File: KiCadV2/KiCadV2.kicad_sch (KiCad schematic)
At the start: 52 parts, among them J1 USB_C_Receptacle_PowerOnly_6P, J3 Screw_Terminal_01x02, J4 Screw_Terminal_01x02, U1 MT3608, U14 74LV08AT14-13, U16 NC7SZ157P6X, U17 MX3502S, U18 MX3502S, U2 74HC595, U26 MX3502S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

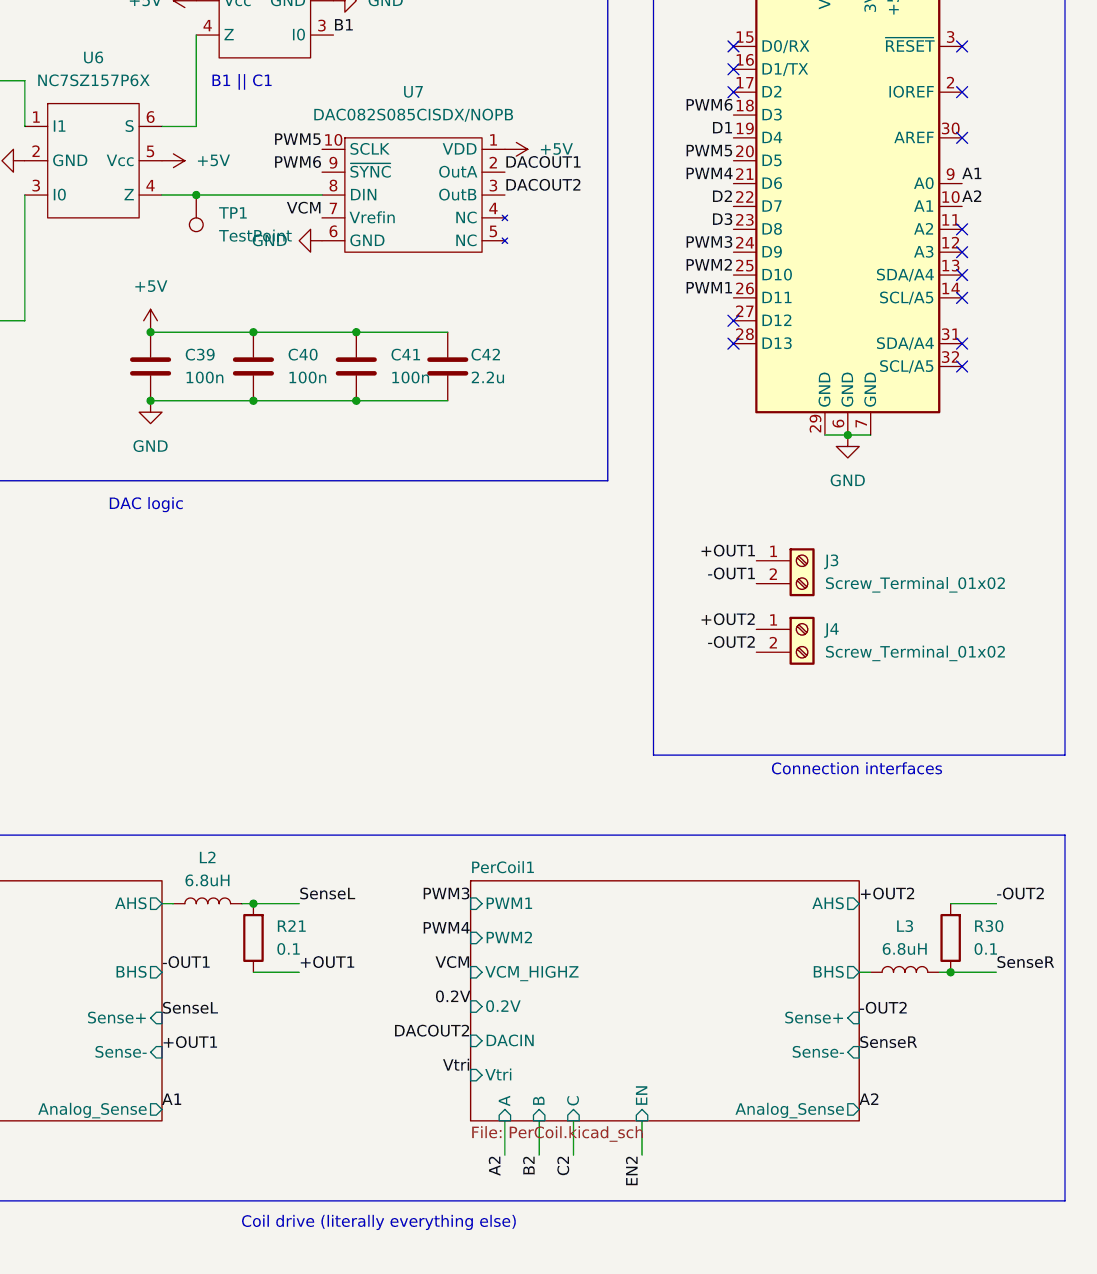
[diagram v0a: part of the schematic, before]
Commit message: minor bug
whoops! Mixed up my Analog pins A1 & A2 with my state pins A1 & A2. That would've been bad 😅
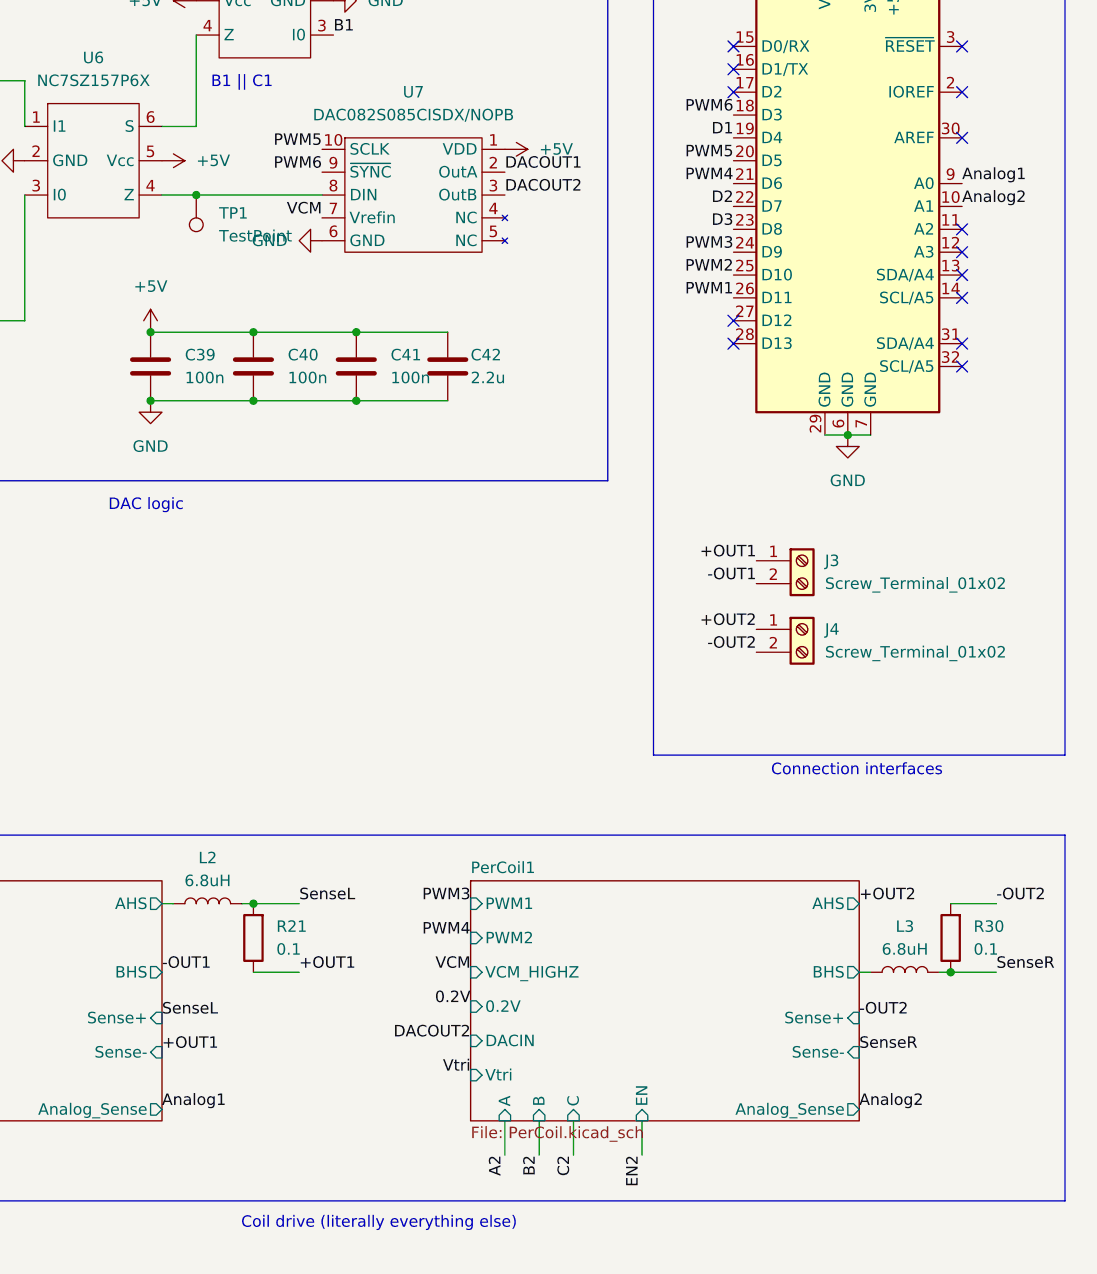
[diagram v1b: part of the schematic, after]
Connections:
- net A1: no longer A1.9 (A0)
- net A2: no longer A1.10 (A1)
- new net Analog1: A1.9 (A0)
- new net Analog2: A1.10 (A1)
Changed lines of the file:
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@@
 		)
 	)
-	(label "A1"
+	(label "Analog1"
 		(at 184.15 148.59 0)
 		(effects
@@
 		)
 	)
+	(label "Analog2"
+		(at 273.05 48.26 0)
+		(effects
+			(font
+				(size 1.27 1.27)
+			)
+			(justify left bottom)
+		)
+	)
 	(label "-OUT1"
 		(at 250.19 90.17 180)
@@
 		)
 	)
-	(label "A2"
-		(at 273.05 48.26 0)
-		(effects
-			(font
-				(size 1.27 1.27)
-			)
-			(justify left bottom)
-		)
-	)
 	(label "VCM"
 		(at 218.44 133.35 180)
@@
 	(label "C2"
 		(at 113.03 46.99 0)
-		(effects
-			(font
-				(size 1.27 1.27)
-			)
-			(justify left bottom)
-		)
-	)
-	(label "A1"
-		(at 273.05 45.72 0)
 		(effects
 			(font
@@
 	)
 	(label "SenseR"
+		(at 276.86 133.35 0)
+		(effects
+			(font
+				(size 1.27 1.27)
+			)
+			(justify left bottom)
+		)
+	)
+	(label "SenseR"
 		(at 261.62 142.24 0)
-		(effects
-			(font
-				(size 1.27 1.27)
-			)
-			(justify left bottom)
-		)
-	)
-	(label "SenseR"
-		(at 276.86 133.35 0)
 		(effects
 			(font
@@
 		)
 	)
+	(label "Analog1"
+		(at 273.05 45.72 0)
+		(effects
+			(font
+				(size 1.27 1.27)
+			)
+			(justify left bottom)
+		)
+	)
 	(label "-OUT2"
 		(at 261.62 138.43 0)
@@
 		)
 	)
-	(label "A2"
+	(label "Analog2"
 		(at 261.62 148.59 0)
 		(effects

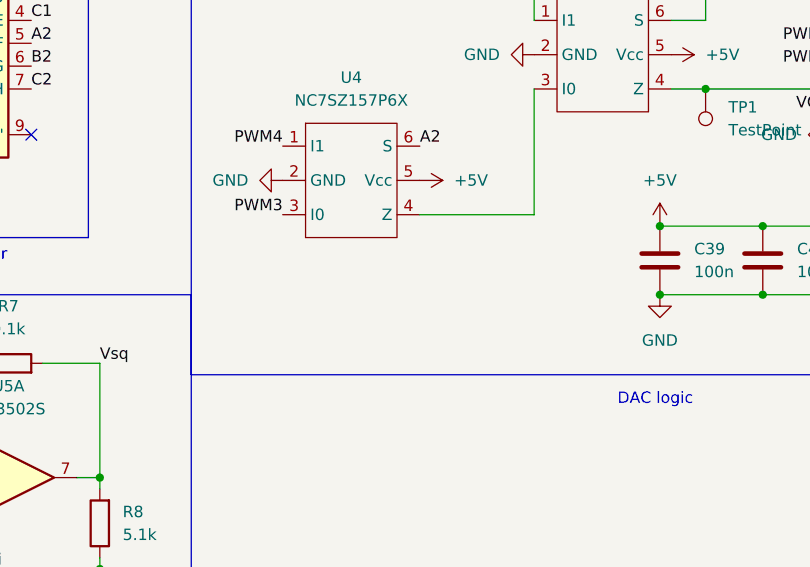
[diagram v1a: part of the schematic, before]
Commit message: DAC logic
- Internal connections done
- Spacing, shorts, nets, etc verified
- Grouped
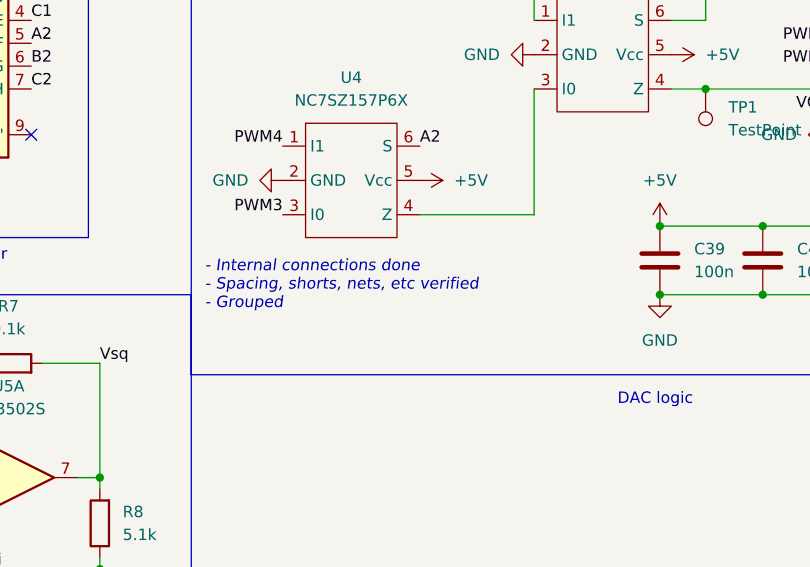
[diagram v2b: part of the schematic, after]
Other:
- note added: "- Internal connections done - Spacing, shorts, nets, etc verified - Grouped"
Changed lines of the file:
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@@
+		)
+	)
+	(text "- Internal connections done\n- Spacing, shorts, nets, etc verified\n- Grouped"
+		(exclude_from_sim no)
+		(at 132.334 68.834 0)
+		(effects
+			(font
+				(size 1.27 1.27)
+				(italic yes)
+				(color 0 194 0 1)
+			)
+			(justify left)
 		)
 	)

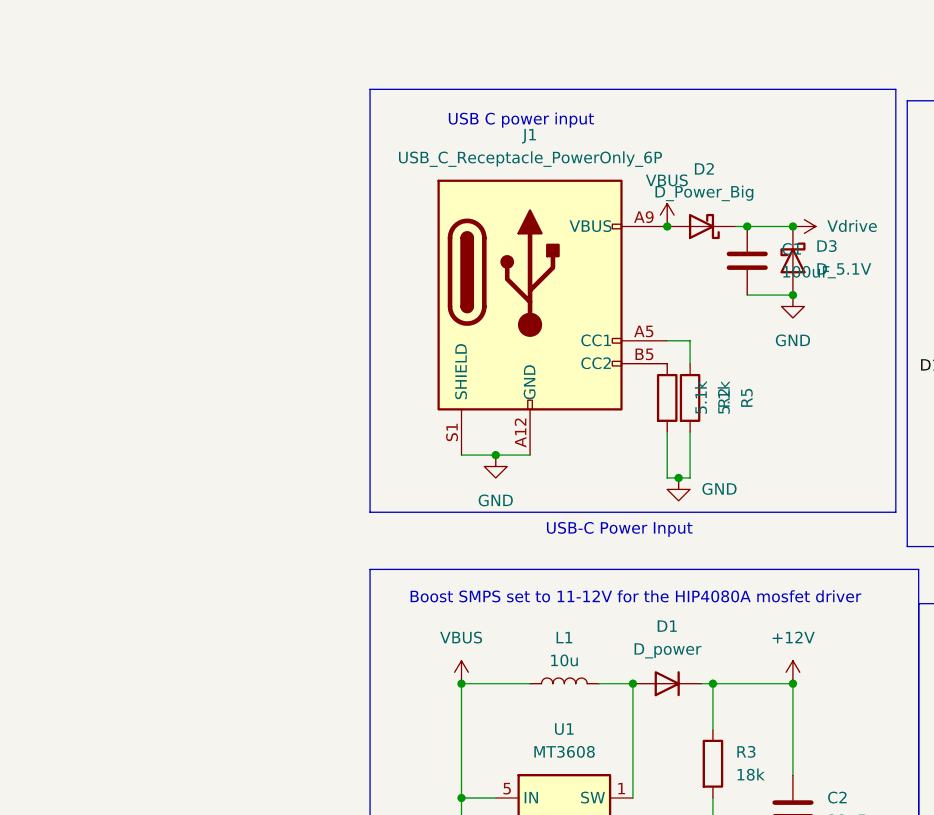
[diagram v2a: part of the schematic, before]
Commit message: USBC power & Boost SMPS done
- Internal connections done
- Spacing, shorts, nets, etc verified
- Grouped
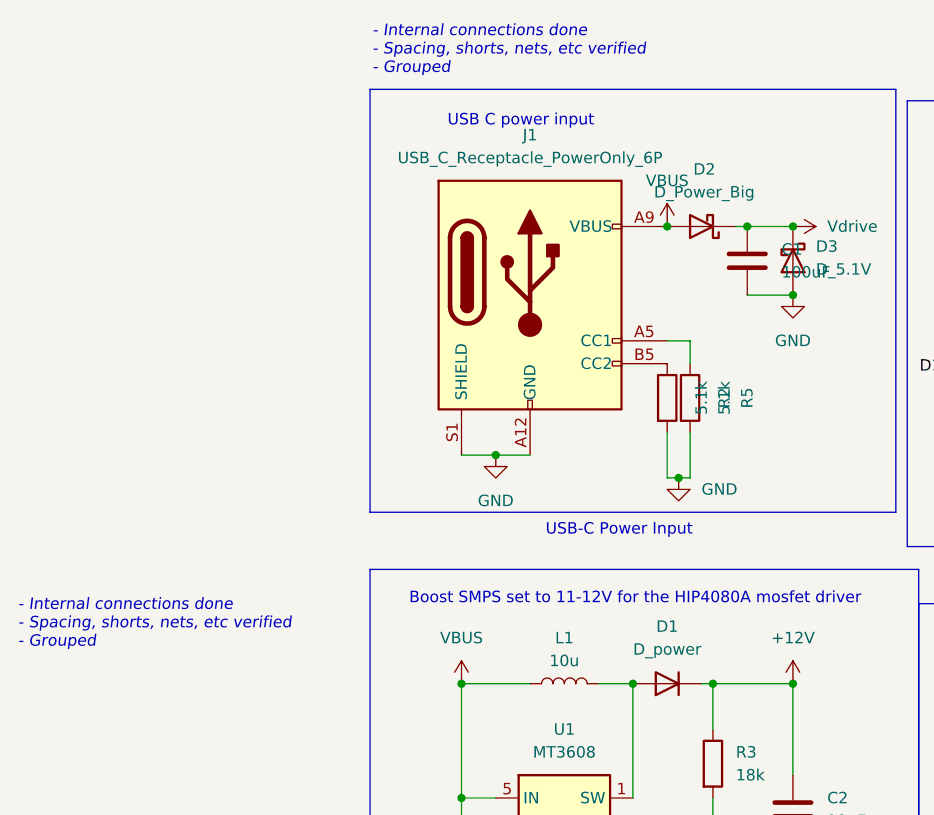
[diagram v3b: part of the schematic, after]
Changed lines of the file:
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@@
+		)
+	)
+	(text "- Internal connections done\n- Spacing, shorts, nets, etc verified\n- Grouped"
+		(exclude_from_sim no)
+		(at -26.416 72.136 0)
+		(effects
+			(font
+				(size 1.27 1.27)
+				(italic yes)
+				(color 0 194 0 1)
+			)
+			(justify left)
 		)
 	)
@@
 		)
 	)
+	(text "- Internal connections done\n- Spacing, shorts, nets, etc verified\n- Grouped"
+		(exclude_from_sim no)
+		(at 12.954 8.382 0)
+		(effects
+			(font
+				(size 1.27 1.27)
+				(italic yes)
+				(color 0 194 0 1)
+			)
+			(justify left)
+		)
+	)

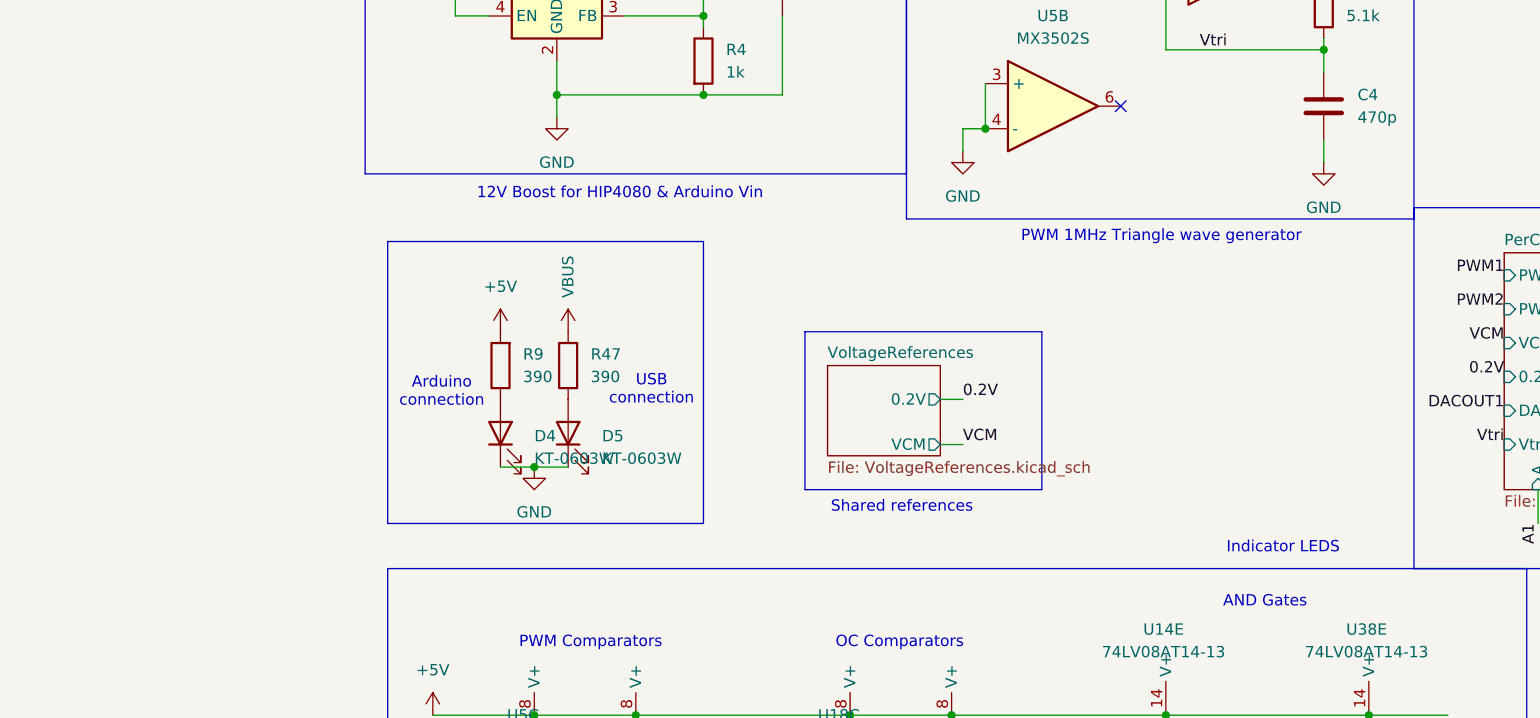
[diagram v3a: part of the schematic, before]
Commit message: Triangle wave done
- Internal connections done
- Spacing, shorts, nets, etc verified
- Grouped
*Doesn't fit now...
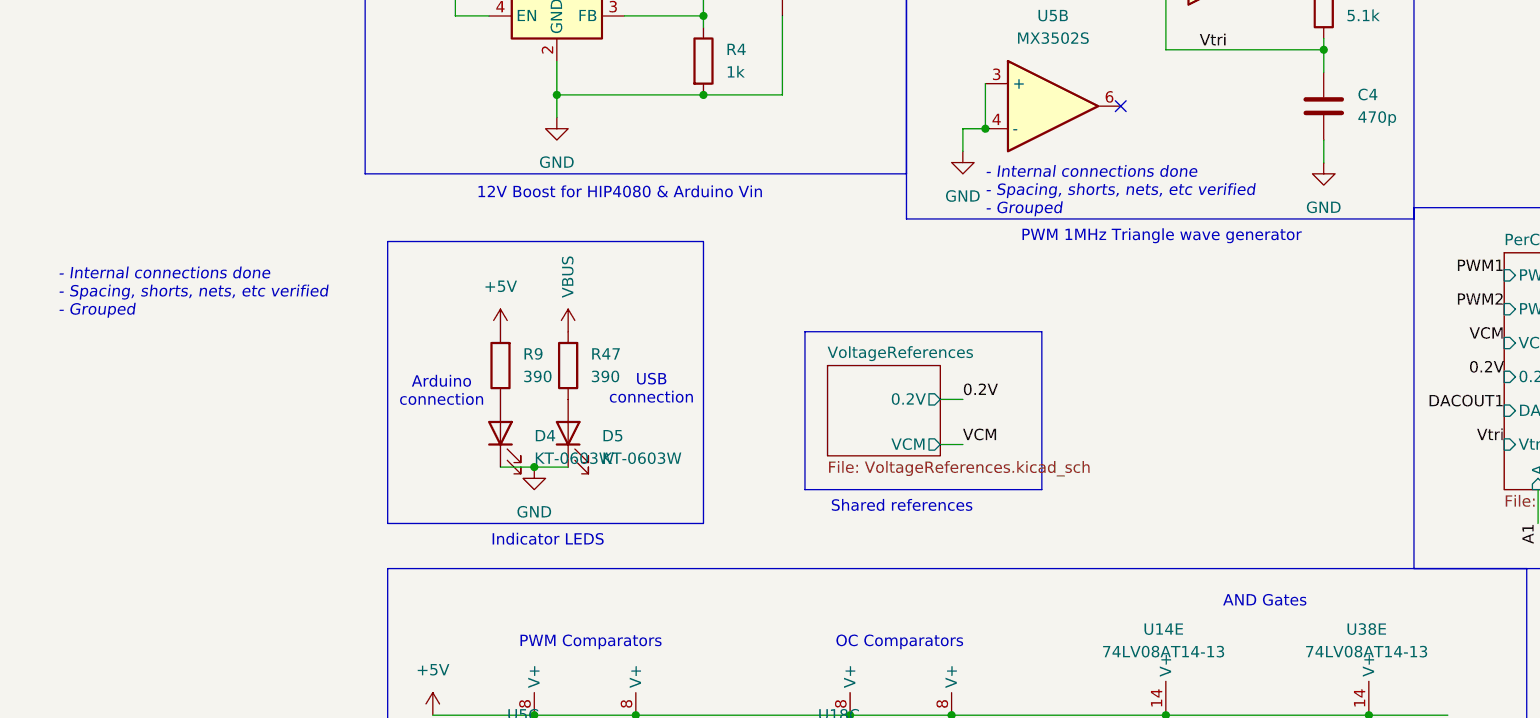
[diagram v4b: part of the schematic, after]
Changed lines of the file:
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@@
+		)
+	)
+	(text "- Internal connections done\n- Spacing, shorts, nets, etc verified\n- Grouped"
+		(exclude_from_sim no)
+		(at 82.55 116.332 0)
+		(effects
+			(font
+				(size 1.27 1.27)
+				(italic yes)
+				(color 0 194 0 1)
+			)
+			(justify left)
 		)
 	)
@@
 	(text "Indicator LEDS"
 		(exclude_from_sim no)
-		(at 116.078 156.464 0)
+		(at 33.274 155.702 0)
 		(effects
 			(font
@@
 		)
 	)
+	(text "- Internal connections done\n- Spacing, shorts, nets, etc verified\n- Grouped"
+		(exclude_from_sim no)
+		(at -21.844 127.762 0)
+		(effects
+			(font
+				(size 1.27 1.27)
+				(italic yes)
+				(color 0 194 0 1)
+			)
+			(justify left)
+		)
+	)

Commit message: Bunchhh of shit
PCB looking gooood
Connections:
- net PWM1: now also A1.20 (D5); no longer A1.26 (D11)
- net PWM2: now also A1.18 (D3); no longer A1.25 (D10)
- net PWM5: now also A1.26 (D11); no longer A1.20 (D5)
- net PWM6: now also A1.25 (D10); no longer A1.18 (D3)
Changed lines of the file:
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@@
 		)
 	)
-	(label "PWM6"
+	(label "PWM2"
 		(at 247.65 38.1 180)
 		(effects
@@
 		)
 	)
-	(label "PWM5"
+	(label "PWM1"
 		(at 247.65 43.18 180)
 		(effects
@@
 		)
 	)
-	(label "PWM1"
+	(label "PWM5"
 		(at 247.65 58.42 180)
 		(effects
@@
 		)
 	)
-	(label "PWM2"
+	(label "PWM6"
 		(at 247.65 55.88 180)
 		(effects

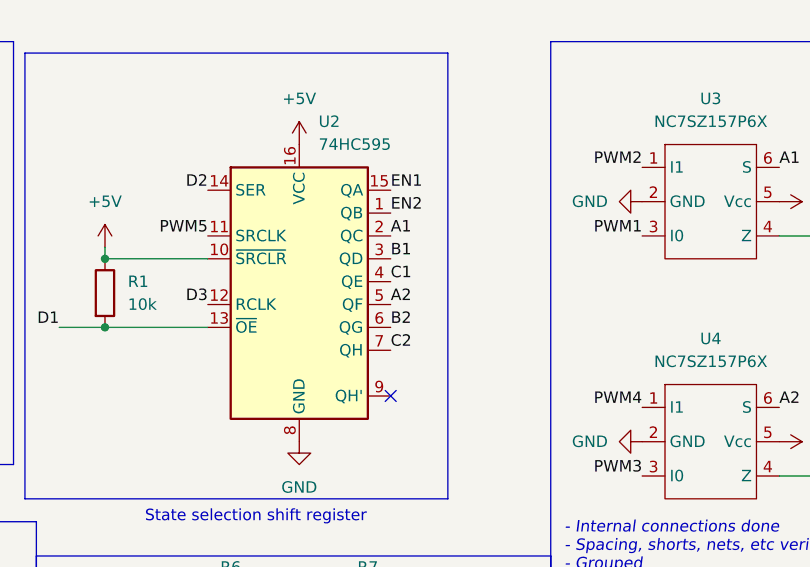
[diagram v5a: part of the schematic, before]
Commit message: Only GND via stitching left!!!
OMG OMG OMG PLEASE NO HUGE ERRORS
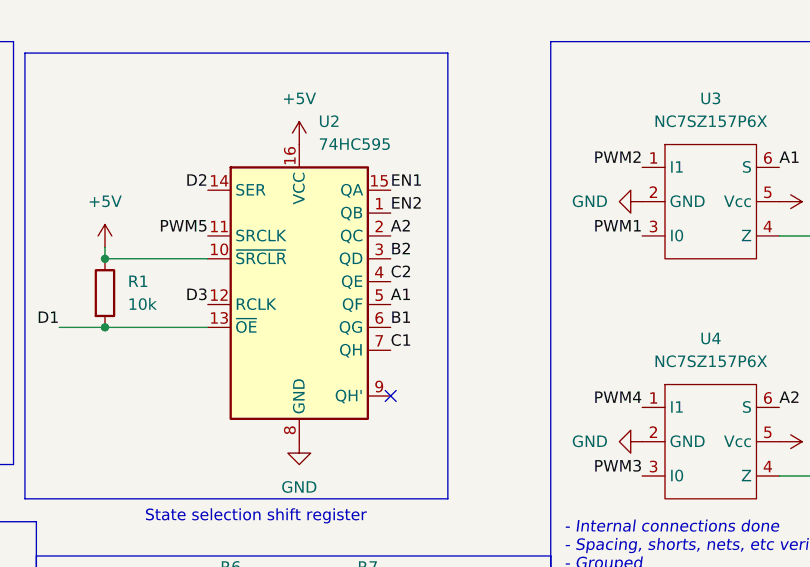
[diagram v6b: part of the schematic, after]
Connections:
- net A1: now also U2.5 (QF); no longer U2.2 (QC)
- net A2: now also U2.2 (QC); no longer U2.5 (QF)
- net B1: now also U2.6 (QG); no longer U2.3 (QD)
- net B2: now also U2.3 (QD); no longer U2.6 (QG)
- net C1: now also U2.7 (QH); no longer U2.4 (QE)
- net C2: now also U2.4 (QE); no longer U2.7 (QH)
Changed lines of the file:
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@@
 	)
 	(label "A1"
+		(at 113.03 41.91 0)
+		(effects
+			(font
+				(size 1.27 1.27)
+			)
+			(justify left bottom)
+		)
+	)
+	(label "B1"
+		(at 113.03 44.45 0)
+		(effects
+			(font
+				(size 1.27 1.27)
+			)
+			(justify left bottom)
+		)
+	)
+	(label "C1"
+		(at 113.03 46.99 0)
+		(effects
+			(font
+				(size 1.27 1.27)
+			)
+			(justify left bottom)
+		)
+	)
+	(label "A2"
 		(at 113.03 34.29 0)
 		(effects
@@
 		)
 	)
-	(label "B1"
+	(label "B2"
 		(at 113.03 36.83 0)
-		(effects
-			(font
-				(size 1.27 1.27)
-			)
-			(justify left bottom)
-		)
-	)
-	(label "C1"
-		(at 113.03 39.37 0)
-		(effects
-			(font
-				(size 1.27 1.27)
-			)
-			(justify left bottom)
-		)
-	)
-	(label "A2"
-		(at 113.03 41.91 0)
-		(effects
-			(font
-				(size 1.27 1.27)
-			)
-			(justify left bottom)
-		)
-	)
-	(label "B2"
-		(at 113.03 44.45 0)
 		(effects
 			(font
@@
 	)
 	(label "C2"
-		(at 113.03 46.99 0)
+		(at 113.03 39.37 0)
 		(effects
 			(font
